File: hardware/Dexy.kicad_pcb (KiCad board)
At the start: 2 copper layers, 111.5 x 108.2 mm, 78 parts, among them J1 WQP-PJ398, J10 Main_Left, J2 WQP-PJ398, J3 WQP-PJ398, J4 WQP-PJ398, J5 WQP-PJ398, J6 Conn_Eurorack_16, J7 Controls_Left, J8 Main_Right, J9 Controls_Right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

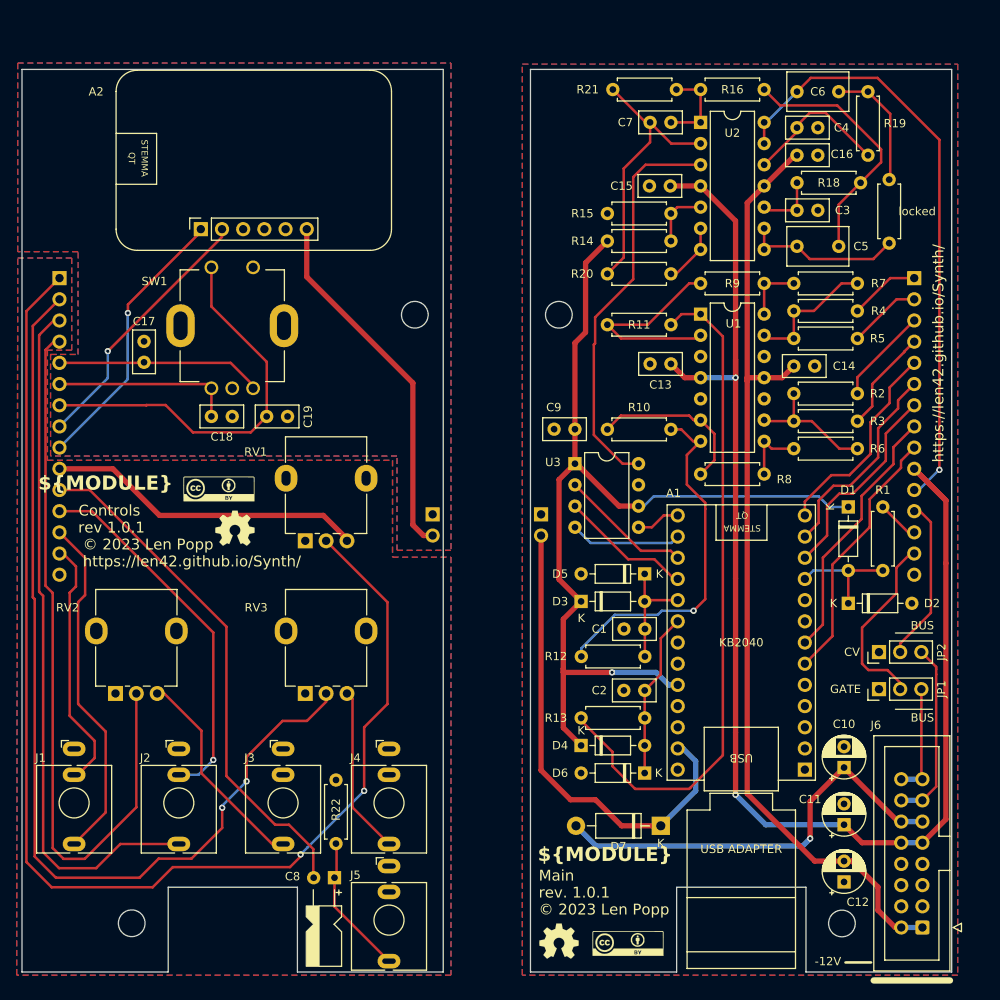
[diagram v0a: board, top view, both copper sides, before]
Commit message: hardware: PCB layout alignment changed to match template
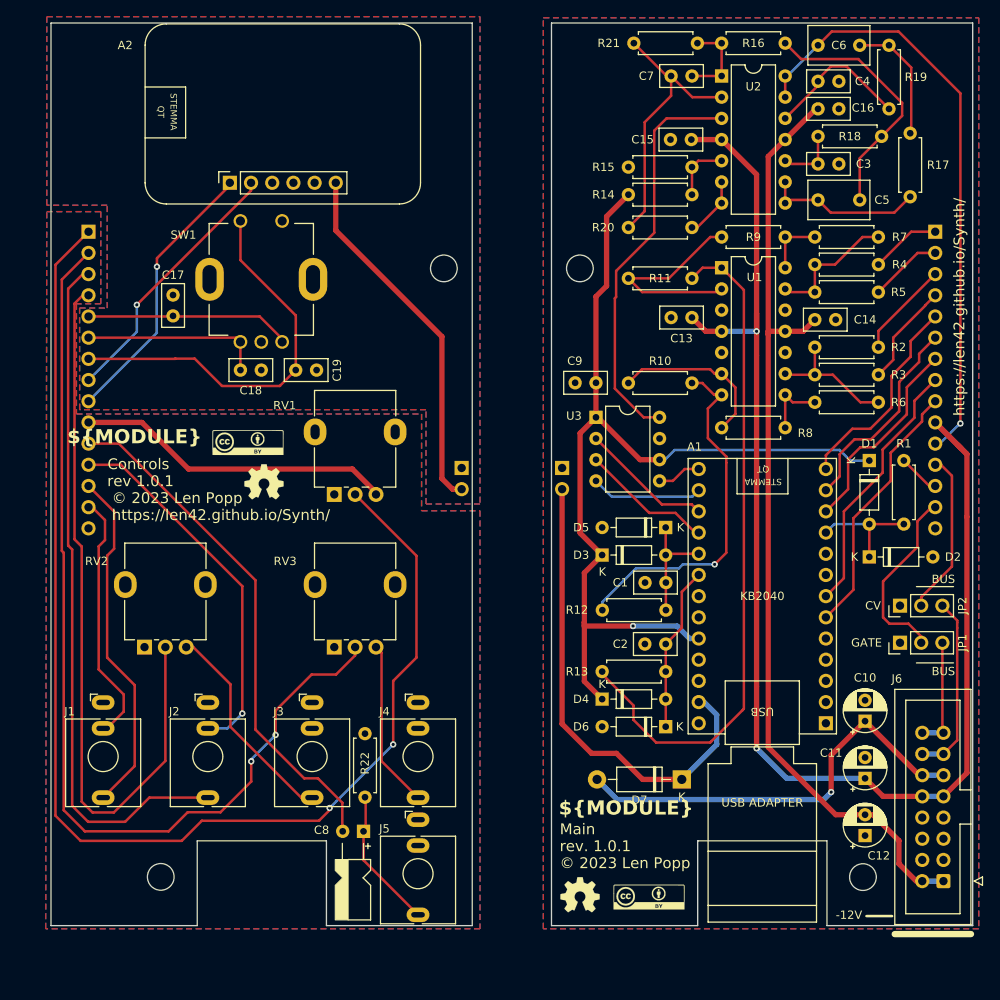
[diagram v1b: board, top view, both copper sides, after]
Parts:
- moved RV1 6.56 mm to (134.0, 86.5)
- moved RV3 6.56 mm to (134.0, 104.8)
- moved C8 6.56 mm to (135.0, 126.9)
- moved A2 6.56 mm to (125.2, 40.8)
- moved C18 6.56 mm to (122.7, 71.6)
- moved G4 6.56 mm to (125.5, 85.0)
- moved H2 6.56 mm to (113.2, 132.4)
- moved J7 6.56 mm to (104.5, 55.0)
- moved J3 6.56 mm to (131.3, 111.5)
- moved C17 6.56 mm to (114.6, 65.1)
- moved C19 6.56 mm to (129.3, 71.6)
- moved H1 6.56 mm to (147.1, 59.4)
- moved J9 6.56 mm to (149.2, 83.3)
- moved R22 6.56 mm to (137.6, 122.8)
- moved RV2 6.56 mm to (111.2, 104.8)
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- renumbered locked to R17
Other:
- board size 111.5 x 108.2 mm -> 110.5 x 108.2 mm
